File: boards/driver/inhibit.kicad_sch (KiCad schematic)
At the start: 11 parts, among them Q34 MMBT2222, Q35 MMBT2222

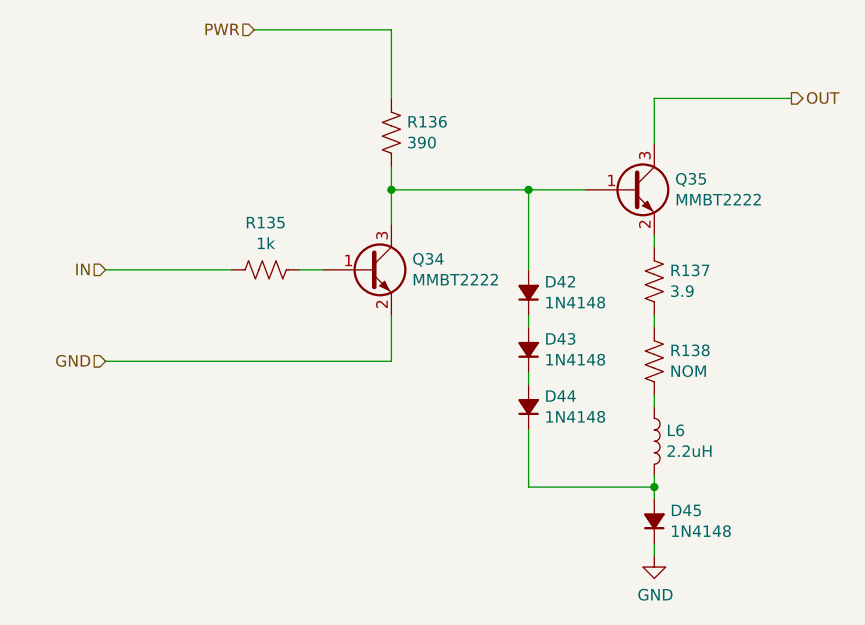
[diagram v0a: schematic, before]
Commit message: Driver: Added a 5V->3.3V LDO to replace the reversed cmod header, added jumpers for the 200R parallel returns, and renamed subcircuit ports to avoid unexpected ground connections.
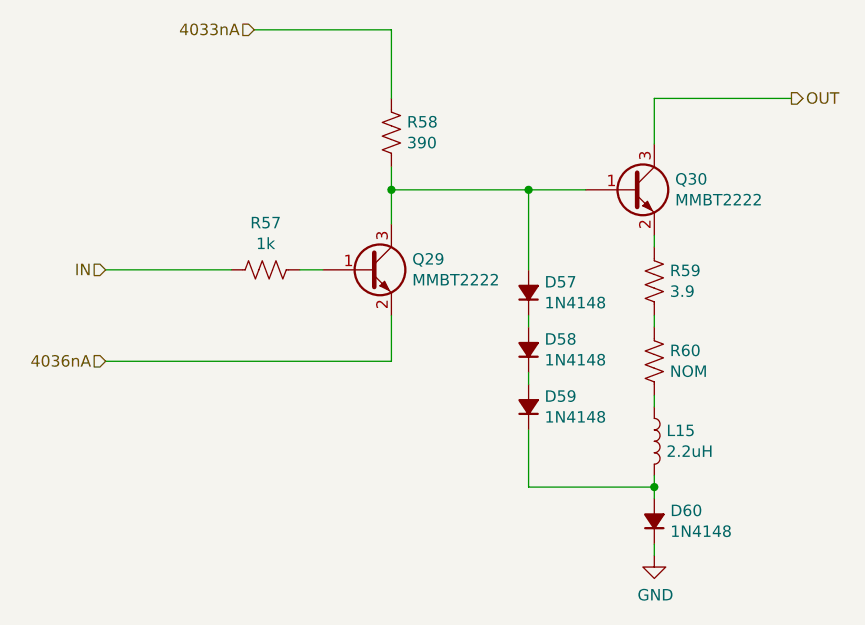
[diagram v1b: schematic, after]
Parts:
- renumbered D42 to D57, D43 to D58, D44 to D59, D45 to D60, L6 to L15, Q34 to Q29, Q35 to Q30, R135 to R57, R136 to R58, R137 to R59, R138 to R60
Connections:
- net GND: no longer Q29.2 (E)
- net PWR renamed 4033nA
- new net 4036nA: Q29.2 (E)
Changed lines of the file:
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@@
     (effects (font (size 1.27 1.27)) (justify right))
   )
-  (hierarchical_label "GND" (shape input) (at 74.93 100.33 180)
+  (hierarchical_label "4036nA" (shape input) (at 74.93 100.33 180)
     (effects (font (size 1.27 1.27)) (justify right))
   )
-  (hierarchical_label "PWR" (shape input) (at 91.44 63.5 180)
+  (hierarchical_label "4033nA" (shape input) (at 91.44 63.5 180)
     (effects (font (size 1.27 1.27)) (justify right))
   )
@@
   (symbol (lib_id "Device:R_US") (at 92.71 90.17 270)
     (in_bom yes) (on_board yes)
-    (property "Reference" "R135" (id 0) (at 92.71 84.963 90))
+    (property "Reference" "R57" (id 0) (at 92.71 84.963 90))
     (property "Value" "1k" (id 1) (at 92.71 87.2744 90))
     (property "Footprint" "Resistor_SMD:R_0603_1608Metric" (id 2) (at 92.456 91.186 90)
@@
   (symbol (lib_id "Device:Q_NPN_BEC") (at 104.14 90.17 0)
     (in_bom yes) (on_board yes)
-    (property "Reference" "Q34" (id 0) (at 108.9914 89.0016 0)
+    (property "Reference" "Q29" (id 0) (at 108.9914 89.0016 0)
       (effects (font (size 1.27 1.27)) (justify left))
     )
@@
   (symbol (lib_id "Device:D_Small_Filled") (at 121.92 105.41 90)
     (in_bom yes) (on_board yes)
-    (property "Reference" "D44" (id 0) (at 123.698 104.2416 90)
+    (property "Reference" "D59" (id 0) (at 123.698 104.2416 90)
       (effects (font (size 1.27 1.27)) (justify right))
     )
@@
   (symbol (lib_id "Device:D_Small_Filled") (at 121.92 99.06 90)
     (in_bom yes) (on_board yes)
-    (property "Reference" "D43" (id 0) (at 123.698 97.8916 90)
+    (property "Reference" "D58" (id 0) (at 123.698 97.8916 90)
       (effects (font (size 1.27 1.27)) (justify right))
     )
@@
   (symbol (lib_id "Device:D_Small_Filled") (at 121.92 92.71 90)
     (in_bom yes) (on_board yes)
-    (property "Reference" "D42" (id 0) (at 123.698 91.5416 90)
+    (property "Reference" "D57" (id 0) (at 123.698 91.5416 90)
       (effects (font (size 1.27 1.27)) (justify right))
     )
@@
   (symbol (lib_id "power:GND") (at 135.89 121.92 0)
     (in_bom yes) (on_board yes)
-    (property "Reference" "#PWR086" (id 0) (at 135.89 128.27 0)
+    (property "Reference" "#PWR015" (id 0) (at 135.89 128.27 0)
       (effects (font (size 1.27 1.27)) hide)
     )
@@
   (symbol (lib_id "Device:Q_NPN_BEC") (at 133.35 81.28 0)
     (in_bom yes) (on_board yes)
-    (property "Reference" "Q35" (id 0) (at 138.2014 80.1116 0)
+    (property "Reference" "Q30" (id 0) (at 138.2014 80.1116 0)
       (effects (font (size 1.27 1.27)) (justify left))
     )
@@
   (symbol (lib_id "Device:R_US") (at 135.89 91.44 0)
     (in_bom yes) (on_board yes)
-    (property "Reference" "R137" (id 0) (at 137.6172 90.2716 0)
+    (property "Reference" "R59" (id 0) (at 137.6172 90.2716 0)
       (effects (font (size 1.27 1.27)) (justify left))
     )
@@
   (symbol (lib_id "Device:L") (at 135.89 109.22 0)
     (in_bom yes) (on_board yes)
-    (property "Reference" "L6" (id 0) (at 137.2362 108.0516 0)
+    (property "Reference" "L15" (id 0) (at 137.2362 108.0516 0)
       (effects (font (size 1.27 1.27)) (justify left))
     )
@@
   (symbol (lib_id "Device:R_US") (at 106.68 74.93 0)
     (in_bom yes) (on_board yes)
-    (property "Reference" "R136" (id 0) (at 108.4072 73.7616 0)
+    (property "Reference" "R58" (id 0) (at 108.4072 73.7616 0)
       (effects (font (size 1.27 1.27)) (justify left))
     )
@@
   (symbol (lib_id "Device:D_Small_Filled") (at 135.89 118.11 90)
     (in_bom yes) (on_board yes)
-    (property "Reference" "D45" (id 0) (at 137.668 116.9416 90)
+    (property "Reference" "D60" (id 0) (at 137.668 116.9416 90)
       (effects (font (size 1.27 1.27)) (justify right))
     )
@@
   (symbol (lib_id "Device:R_US") (at 135.89 100.33 0)
     (in_bom yes) (on_board yes)
-    (property "Reference" "R138" (id 0) (at 137.6172 99.1616 0)
-      (effects (font (size 1.27 1.27)) (justify left))
-    )
+    (property "Reference" "R60" (id 0) (at 137.6172 99.1616 0)
+      (effects (font (size 1.27 1.27)) (justify left))
+    )

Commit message: Driver: incorporated most changes from the test board, and began layout
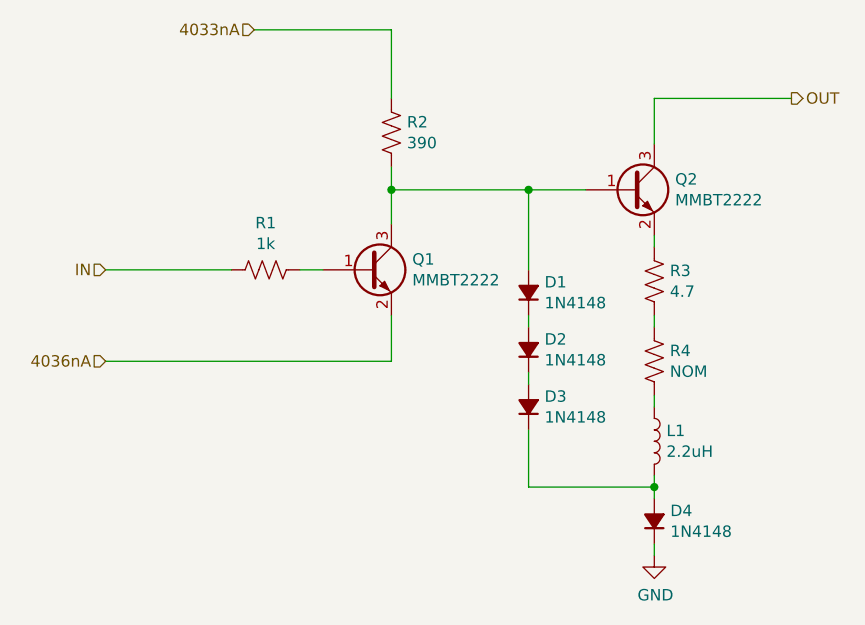
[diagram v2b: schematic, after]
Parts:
- D1: renamed from D57; footprint Diode_SMD:D_SOD-323 -> lachesis:D_SOD-323
- D2: renamed from D58; footprint Diode_SMD:D_SOD-323 -> lachesis:D_SOD-323
- D3: renamed from D59; footprint Diode_SMD:D_SOD-323 -> lachesis:D_SOD-323
- D4: renamed from D60; footprint Diode_SMD:D_SOD-323 -> lachesis:D_SOD-323
- L1: renamed from L15; footprint Inductor_SMD:L_1812_4532Metric -> lachesis:API_Delevan_1812R
- R3: renamed from R59; value 3.9 -> 4.7
- renumbered Q29 to Q1, Q30 to Q2, R57 to R1, R58 to R2, R60 to R4
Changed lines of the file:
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@@
     (effects (font (size 1.27 1.27)) (justify left))
   )
-  (symbol (lib_id "Device:R_US") (at 92.71 90.17 270)
-    (in_bom yes) (on_board yes)
-    (property "Reference" "R57" (id 0) (at 92.71 84.963 90))
+  (symbol (lib_id "Device:R_US") (at 92.71 90.17 270) (unit 1)
+    (in_bom yes) (on_board yes)
+    (property "Reference" "R1" (id 0) (at 92.71 84.963 90))
     (property "Value" "1k" (id 1) (at 92.71 87.2744 90))
     (property "Footprint" "Resistor_SMD:R_0603_1608Metric" (id 2) (at 92.456 91.186 90)
@@
     (pin "2")
   )
-  (symbol (lib_id "Device:Q_NPN_BEC") (at 104.14 90.17 0)
-    (in_bom yes) (on_board yes)
-    (property "Reference" "Q29" (id 0) (at 108.9914 89.0016 0)
+  (symbol (lib_id "Device:Q_NPN_BEC") (at 104.14 90.17 0) (unit 1)
+    (in_bom yes) (on_board yes)
+    (property "Reference" "Q1" (id 0) (at 108.9914 89.0016 0)
       (effects (font (size 1.27 1.27)) (justify left))
     )
@@
     (pin "3")
   )
-  (symbol (lib_id "Device:D_Small_Filled") (at 121.92 105.41 90)
-    (in_bom yes) (on_board yes)
-    (property "Reference" "D59" (id 0) (at 123.698 104.2416 90)
+  (symbol (lib_id "Device:D_Small_Filled") (at 121.92 105.41 90) (unit 1)
+    (in_bom yes) (on_board yes)
+    (property "Reference" "D3" (id 0) (at 123.698 104.2416 90)
       (effects (font (size 1.27 1.27)) (justify right))
     )
@@
       (effects (font (size 1.27 1.27)) (justify right))
     )
-    (property "Footprint" "Diode_SMD:D_SOD-323" (id 2) (at 121.92 105.41 90)
+    (property "Footprint" "lachesis:D_SOD-323" (id 2) (at 121.92 105.41 90)
       (effects (font (size 1.27 1.27)) hide)
     )
@@
     (pin "2")
   )
-  (symbol (lib_id "Device:D_Small_Filled") (at 121.92 99.06 90)
-    (in_bom yes) (on_board yes)
-    (property "Reference" "D58" (id 0) (at 123.698 97.8916 90)
+  (symbol (lib_id "Device:D_Small_Filled") (at 121.92 99.06 90) (unit 1)
+    (in_bom yes) (on_board yes)
+    (property "Reference" "D2" (id 0) (at 123.698 97.8916 90)
       (effects (font (size 1.27 1.27)) (justify right))
     )
@@
       (effects (font (size 1.27 1.27)) (justify right))
     )
-    (property "Footprint" "Diode_SMD:D_SOD-323" (id 2) (at 121.92 99.06 90)
+    (property "Footprint" "lachesis:D_SOD-323" (id 2) (at 121.92 99.06 90)
       (effects (font (size 1.27 1.27)) hide)
     )
@@
     (pin "2")
   )
-  (symbol (lib_id "Device:D_Small_Filled") (at 121.92 92.71 90)
-    (in_bom yes) (on_board yes)
-    (property "Reference" "D57" (id 0) (at 123.698 91.5416 90)
+  (symbol (lib_id "Device:D_Small_Filled") (at 121.92 92.71 90) (unit 1)
+    (in_bom yes) (on_board yes)
+    (property "Reference" "D1" (id 0) (at 123.698 91.5416 90)
       (effects (font (size 1.27 1.27)) (justify right))
     )
@@
       (effects (font (size 1.27 1.27)) (justify right))
     )
-    (property "Footprint" "Diode_SMD:D_SOD-323" (id 2) (at 121.92 92.71 90)
+    (property "Footprint" "lachesis:D_SOD-323" (id 2) (at 121.92 92.71 90)
       (effects (font (size 1.27 1.27)) hide)
     )
@@
     (pin "2")
   )
-  (symbol (lib_id "power:GND") (at 135.89 121.92 0)
-    (in_bom yes) (on_board yes)
-    (property "Reference" "#PWR015" (id 0) (at 135.89 128.27 0)
+  (symbol (lib_id "power:GND") (at 135.89 121.92 0) (unit 1)
+    (in_bom yes) (on_board yes)
+    (property "Reference" "#PWR01" (id 0) (at 135.89 128.27 0)
       (effects (font (size 1.27 1.27)) hide)
     )
@@
     (pin "1")
   )
-  (symbol (lib_id "Device:Q_NPN_BEC") (at 133.35 81.28 0)
-    (in_bom yes) (on_board yes)
-    (property "Reference" "Q30" (id 0) (at 138.2014 80.1116 0)
+  (symbol (lib_id "Device:Q_NPN_BEC") (at 133.35 81.28 0) (unit 1)
+    (in_bom yes) (on_board yes)
+    (property "Reference" "Q2" (id 0) (at 138.2014 80.1116 0)
       (effects (font (size 1.27 1.27)) (justify left))
     )
@@
     (pin "3")
   )
-  (symbol (lib_id "Device:R_US") (at 135.89 91.44 0)
-    (in_bom yes) (on_board yes)
-    (property "Reference" "R59" (id 0) (at 137.6172 90.2716 0)
-      (effects (font (size 1.27 1.27)) (justify left))
-    )
-    (property "Value" "3.9" (id 1) (at 137.6172 92.583 0)
+  (symbol (lib_id "Device:R_US") (at 135.89 91.44 0) (unit 1)
+    (in_bom yes) (on_board yes)
+    (property "Reference" "R3" (id 0) (at 137.6172 90.2716 0)
+      (effects (font (size 1.27 1.27)) (justify left))
+    )
+    (property "Value" "4.7" (id 1) (at 137.6172 92.583 0)
       (effects (font (size 1.27 1.27)) (justify left))
     )
@@
     (pin "2")
   )
-  (symbol (lib_id "Device:L") (at 135.89 109.22 0)
-    (in_bom yes) (on_board yes)
-    (property "Reference" "L15" (id 0) (at 137.2362 108.0516 0)
+  (symbol (lib_id "Device:L") (at 135.89 109.22 0) (unit 1)
+    (in_bom yes) (on_board yes)
+    (property "Reference" "L1" (id 0) (at 137.2362 108.0516 0)
       (effects (font (size 1.27 1.27)) (justify left))
     )
@@
       (effects (font (size 1.27 1.27)) (justify left))
     )
-    (property "Footprint" "Inductor_SMD:L_1812_4532Metric" (id 2) (at 135.89 109.22 0)
+    (property "Footprint" "lachesis:API_Delevan_1812R" (id 2) (at 135.89 109.22 0)
       (effects (font (size 1.27 1.27)) hide)
     )
@@
     (pin "2")
   )
-  (symbol (lib_id "Device:R_US") (at 106.68 74.93 0)
-    (in_bom yes) (on_board yes)
-    (property "Reference" "R58" (id 0) (at 108.4072 73.7616 0)
+  (symbol (lib_id "Device:R_US") (at 106.68 74.93 0) (unit 1)
+    (in_bom yes) (on_board yes)
+    (property "Reference" "R2" (id 0) (at 108.4072 73.7616 0)
       (effects (font (size 1.27 1.27)) (justify left))
     )
@@
     (pin "2")
   )
-  (symbol (lib_id "Device:D_Small_Filled") (at 135.89 118.11 90)
-    (in_bom yes) (on_board yes)
-    (property "Reference" "D60" (id 0) (at 137.668 116.9416 90)
+  (symbol (lib_id "Device:D_Small_Filled") (at 135.89 118.11 90) (unit 1)
+    (in_bom yes) (on_board yes)
+    (property "Reference" "D4" (id 0) (at 137.668 116.9416 90)
       (effects (font (size 1.27 1.27)) (justify right))
     )
@@
       (effects (font (size 1.27 1.27)) (justify right))
     )
-    (property "Footprint" "Diode_SMD:D_SOD-323" (id 2) (at 135.89 118.11 90)
+    (property "Footprint" "lachesis:D_SOD-323" (id 2) (at 135.89 118.11 90)
       (effects (font (size 1.27 1.27)) hide)
     )
@@
     (pin "2")
   )
-  (symbol (lib_id "Device:R_US") (at 135.89 100.33 0)
-    (in_bom yes) (on_board yes)
-    (property "Reference" "R60" (id 0) (at 137.6172 99.1616 0)
-      (effects (font (size 1.27 1.27)) (justify left))
-    )
+  (symbol (lib_id "Device:R_US") (at 135.89 100.33 0) (unit 1)
+    (in_bom yes) (on_board yes)
+    (property "Reference" "R4" (id 0) (at 137.6172 99.1616 0)
+      (effects (font (size 1.27 1.27)) (justify left))
+    )

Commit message: Driver: minor schematic cleanup and populated all of the BOM except for resistors
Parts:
- D1, D2, D3, D4: MPN (none) -> 1N4148WS; Manufacturer (none) -> SMC Diode Solutions; Package (none) -> SOD-323; Rating (none) -> 300mA
- L1: MPN (none) -> 1812R-222J; Manufacturer (none) -> API Delevan Inc; Package (none) -> 1812
- Q1, Q2: MPN (none) -> MMBT2222ALT1HTSA1; Manufacturer (none) -> Infineon Technologies; Package (none) -> SOT-23-3
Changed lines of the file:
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@@
+      (effects (font (size 1.27 1.27)) hide)
+    )
+    (property "MPN" "MMBT2222ALT1HTSA1" (id 6) (at 104.14 90.17 0)
+      (effects (font (size 1.27 1.27)) hide)
+    )
+    (property "Manufacturer" "Infineon Technologies" (id 7) (at 104.14 90.17 0)
+      (effects (font (size 1.27 1.27)) hide)
+    )
+    (property "Description" "TRANS NPN 40V 0.6A SOT-23" (id 8) (at 104.14 90.17 0)
+      (effects (font (size 1.27 1.27)) hide)
+    )
+    (property "Package" "SOT-23-3" (id 9) (at 104.14 90.17 0)
       (effects (font (size 1.27 1.27)) hide)
     )
@@
       (effects (font (size 1.27 1.27)) hide)
     )
+    (property "MPN" "1N4148WS" (id 6) (at 121.92 105.41 0)
+      (effects (font (size 1.27 1.27)) hide)
+    )
+    (property "Manufacturer" "SMC Diode Solutions" (id 7) (at 121.92 105.41 0)
+      (effects (font (size 1.27 1.27)) hide)
+    )
+    (property "Description" "DIODE GEN PURP 75V 300MA SOD323" (id 8) (at 121.92 105.41 0)
+      (effects (font (size 1.27 1.27)) hide)
+    )
+    (property "Package" "SOD-323" (id 9) (at 121.92 105.41 0)
+      (effects (font (size 1.27 1.27)) hide)
+    )
+    (property "Rating" "300mA" (id 10) (at 121.92 105.41 0)
+      (effects (font (size 1.27 1.27)) hide)
+    )
     (pin "1")
     (pin "2")
@@
       (effects (font (size 1.27 1.27)) hide)
     )
+    (property "MPN" "1N4148WS" (id 6) (at 121.92 99.06 0)
+      (effects (font (size 1.27 1.27)) hide)
+    )
+    (property "Manufacturer" "SMC Diode Solutions" (id 7) (at 121.92 99.06 0)
+      (effects (font (size 1.27 1.27)) hide)
+    )
+    (property "Description" "DIODE GEN PURP 75V 300MA SOD323" (id 8) (at 121.92 99.06 0)
+      (effects (font (size 1.27 1.27)) hide)
+    )
+    (property "Package" "SOD-323" (id 9) (at 121.92 99.06 0)
+      (effects (font (size 1.27 1.27)) hide)
+    )
+    (property "Rating" "300mA" (id 10) (at 121.92 99.06 0)
+      (effects (font (size 1.27 1.27)) hide)
+    )
     (pin "1")
     (pin "2")
@@
     )
     (property "Digikey" "https://www.digikey.com/en/products/detail/smc-diode-solutions/1N4148WSTR/6022449" (id 5) (at 134.62 90.17 90)
+      (effects (font (size 1.27 1.27)) hide)
+    )
+    (property "MPN" "1N4148WS" (id 6) (at 121.92 92.71 0)
+      (effects (font (size 1.27 1.27)) hide)
+    )
+    (property "Manufacturer" "SMC Diode Solutions" (id 7) (at 121.92 92.71 0)
+      (effects (font (size 1.27 1.27)) hide)
+    )
+    (property "Description" "DIODE GEN PURP 75V 300MA SOD323" (id 8) (at 121.92 92.71 0)
+      (effects (font (size 1.27 1.27)) hide)
+    )
+    (property "Package" "SOD-323" (id 9) (at 121.92 92.71 0)
+      (effects (font (size 1.27 1.27)) hide)
+    )
+    (property "Rating" "300mA" (id 10) (at 121.92 92.71 0)
       (effects (font (size 1.27 1.27)) hide)
     )
@@
       (effects (font (size 1.27 1.27)) hide)
     )
+    (property "MPN" "MMBT2222ALT1HTSA1" (id 6) (at 133.35 81.28 0)
+      (effects (font (size 1.27 1.27)) hide)
+    )
+    (property "Manufacturer" "Infineon Technologies" (id 7) (at 133.35 81.28 0)
+      (effects (font (size 1.27 1.27)) hide)
+    )
+    (property "Description" "TRANS NPN 40V 0.6A SOT-23" (id 8) (at 133.35 81.28 0)
+      (effects (font (size 1.27 1.27)) hide)
+    )
+    (property "Package" "SOT-23-3" (id 9) (at 133.35 81.28 0)
+      (effects (font (size 1.27 1.27)) hide)
+    )
     (pin "1")
     (pin "2")
@@
       (effects (font (size 1.27 1.27)) hide)
     )
+    (property "MPN" "1812R-222J" (id 9) (at 135.89 109.22 0)
+      (effects (font (size 1.27 1.27)) hide)
+    )
+    (property "Manufacturer" "API Delevan Inc" (id 10) (at 135.89 109.22 0)
+      (effects (font (size 1.27 1.27)) hide)
+    )
+    (property "Description" "FIXED IND 2.2UH 535MA 700MOHM SM" (id 11) (at 135.89 109.22 0)
+      (effects (font (size 1.27 1.27)) hide)
+    )
+    (property "Package" "1812" (id 12) (at 135.89 109.22 0)
+      (effects (font (size 1.27 1.27)) hide)
+    )
     (pin "1")
     (pin "2")
@@
       (effects (font (size 1.27 1.27)) hide)
     )
+    (property "MPN" "1N4148WS" (id 6) (at 135.89 118.11 0)
+      (effects (font (size 1.27 1.27)) hide)
+    )
+    (property "Manufacturer" "SMC Diode Solutions" (id 7) (at 135.89 118.11 0)
+      (effects (font (size 1.27 1.27)) hide)
+    )
+    (property "Description" "DIODE GEN PURP 75V 300MA SOD323" (id 8) (at 135.89 118.11 0)
+      (effects (font (size 1.27 1.27)) hide)
+    )
+    (property "Package" "SOD-323" (id 9) (at 135.89 118.11 0)
+      (effects (font (size 1.27 1.27)) hide)
+    )
+    (property "Rating" "300mA" (id 10) (at 135.89 118.11 0)
+      (effects (font (size 1.27 1.27)) hide)
+    )
